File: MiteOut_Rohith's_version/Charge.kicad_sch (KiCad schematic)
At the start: 31 parts, among them J2 JST, SW2 SW_SPST, U5 BQ25185DLHR, U6 INA260, U7 TPS61022

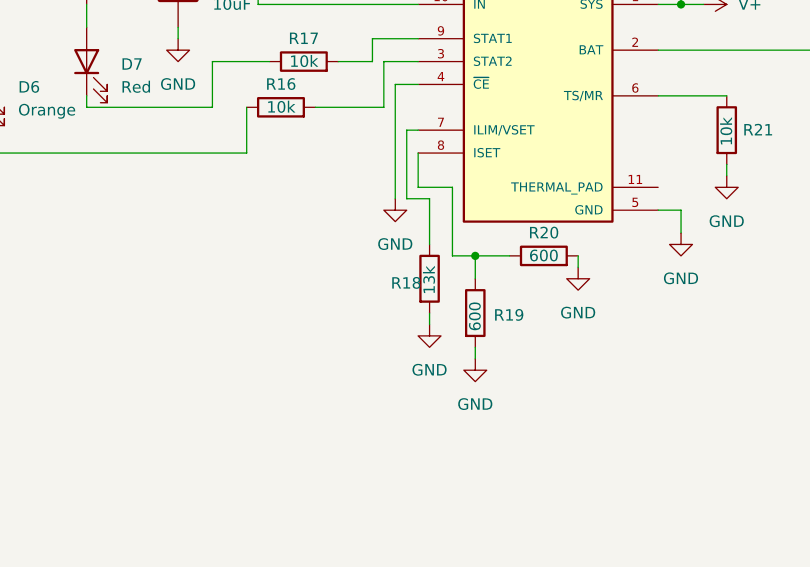
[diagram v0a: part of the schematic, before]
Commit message: Finished MicroSD
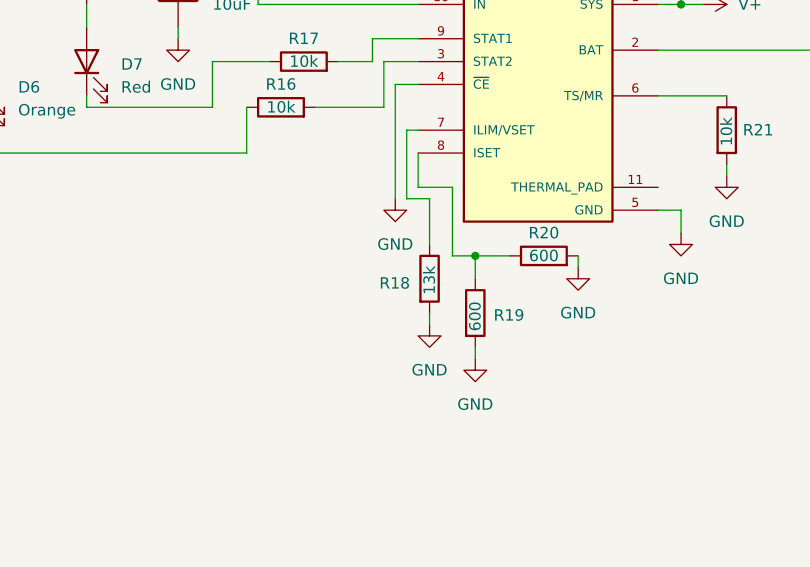
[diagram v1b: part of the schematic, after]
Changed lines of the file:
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@@
 		(dnp no)
 		(property "Reference" "R18"
-			(at 101.092 90.678 0)
+			(at 99.822 90.678 0)
 			(show_name no)
 			(do_not_autoplace no)

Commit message: Full Schematic Draft 1
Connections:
- net ESP_SCL renamed SCK
- net ESP_SDA renamed SDA
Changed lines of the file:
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@@
 		)
 	)
-	(global_label "VIN{slash}Solar+"
+	(hierarchical_label "SDA"
 		(shape input)
-		(at 86.36 41.91 90)
-		(fields_autoplaced yes)
+		(at 199.39 76.2 0)
 		(effects
 			(font
@@
 			(justify left)
 		)
-		(property "Intersheetrefs" "${INTERSHEET_REFS}"
-			(at 86.36 28.0391 90)
-			(hide yes)
-			(show_name no)
-			(do_not_autoplace no)
-			(effects
-				(font
-					(size 1.27 1.27)
-				)
-				(justify left)
-			)
-		)
 	)
-	(global_label "ESP_SCL"
+	(hierarchical_label "SCK"
 		(shape input)
 		(at 199.39 72.39 0)
-		(fields_autoplaced yes)
 		(effects
 			(font
@@
 			(justify left)
 		)
-		(property "Intersheetrefs" "${INTERSHEET_REFS}"
-			(at 210.4789 72.39 0)
-			(hide yes)
-			(show_name no)
-			(do_not_autoplace no)
-			(effects
-				(font
-					(size 1.27 1.27)
-				)
-				(justify left)
-			)
-		)
 	)
-	(global_label "ESP_SDA"
+	(hierarchical_label "VBUS"
 		(shape input)
-		(at 199.39 76.2 0)
-		(fields_autoplaced yes)
+		(at 100.33 41.91 90)
 		(effects
 			(font
@@
 			(justify left)
 		)
-		(property "Intersheetrefs" "${INTERSHEET_REFS}"
-			(at 210.5394 76.2 0)
-			(hide yes)
-			(show_name no)
-			(do_not_autoplace no)
-			(effects
-				(font
-					(size 1.27 1.27)
-				)
-				(justify left)
-			)
-		)
 	)
-	(global_label "VBUS"
+	(hierarchical_label "VIN{slash}Solar+"
 		(shape input)
-		(at 100.33 41.91 90)
-		(fields_autoplaced yes)
+		(at 86.36 41.91 90)
 		(effects
 			(font
@@
 			(justify left)
 		)
-		(property "Intersheetrefs" "${INTERSHEET_REFS}"
-			(at 100.33 34.0262 90)
-			(hide yes)
-			(show_name no)
-			(do_not_autoplace no)
-			(effects
-				(font
-					(size 1.27 1.27)
-				)
-				(justify left)
-			)
-		)
 	)

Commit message: some error fixes
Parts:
- removed D9: NSR0320, symbol Device:D
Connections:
- net at U5.11 (THERMAL_PAD): now also R21.1, U5.6 (TS/MR)
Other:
- moved on the sheet: D10, L2, R21, R22, R26, R27, R28, SW2, U7

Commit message: Fully checked schematic
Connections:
- net VCC is gone; now on net +5V: R23.1, R5.1
- net +5V: now also C10.1, C11.1, C11.2, C12.1, C12.2, C2.1, C2.2, C8.2, C9.1, D10.2 (A), J2.2 (Pin_2), R18.2, R19.2, R20.2, R21.2, R23.2, R26.1, R28.1, R5.2, U5.4 (~{CE}), U5.5 (GND), U6.10 (VS), U6.11 (GND), U6.14 (IN-), U6.15 (IN-), U6.16 (IN-), U6.4 (A1), U6.5 (A0), U6.6 (GND), U7.1 (GND)
- removed net GND: C10.1, C11.1, C11.2, C12.1, C12.2, C2.2, C8.2, C9.1, D10.2 (A), J2.2 (Pin_2), R18.2, R19.2, R20.2, R21.2, R22.2, R23.2, R26.1, R28.1, R5.2, SW2.1 (A), U5.4 (~{CE}), U5.5 (GND), U6.11 (GND), U6.14 (IN-), U6.15 (IN-), U6.16 (IN-), U6.4 (A1), U6.5 (A0), U6.6 (GND), U7.1 (GND)
- net IN+: no longer names the net of C10.2, J2.1 (Pin_1), U5.2 (BAT), U6.1 (IN+), U6.12 (VBUS), U6.2 (IN+), U6.3 (IN+)
- new net: R22.2, SW2.1 (A)
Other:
- moved on the sheet: C2, C9, D10, L2, R22, R26, R27, R28, SW2, U7
